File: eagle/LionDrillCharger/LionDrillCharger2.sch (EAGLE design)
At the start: 25 parts, among them IC1 AT90S2313P, K1 JW1A, K2 JW1A, K3 JW1A, K4 JW1A, T1 BC237, T2 BC237, T3 BC237, T4 BC237

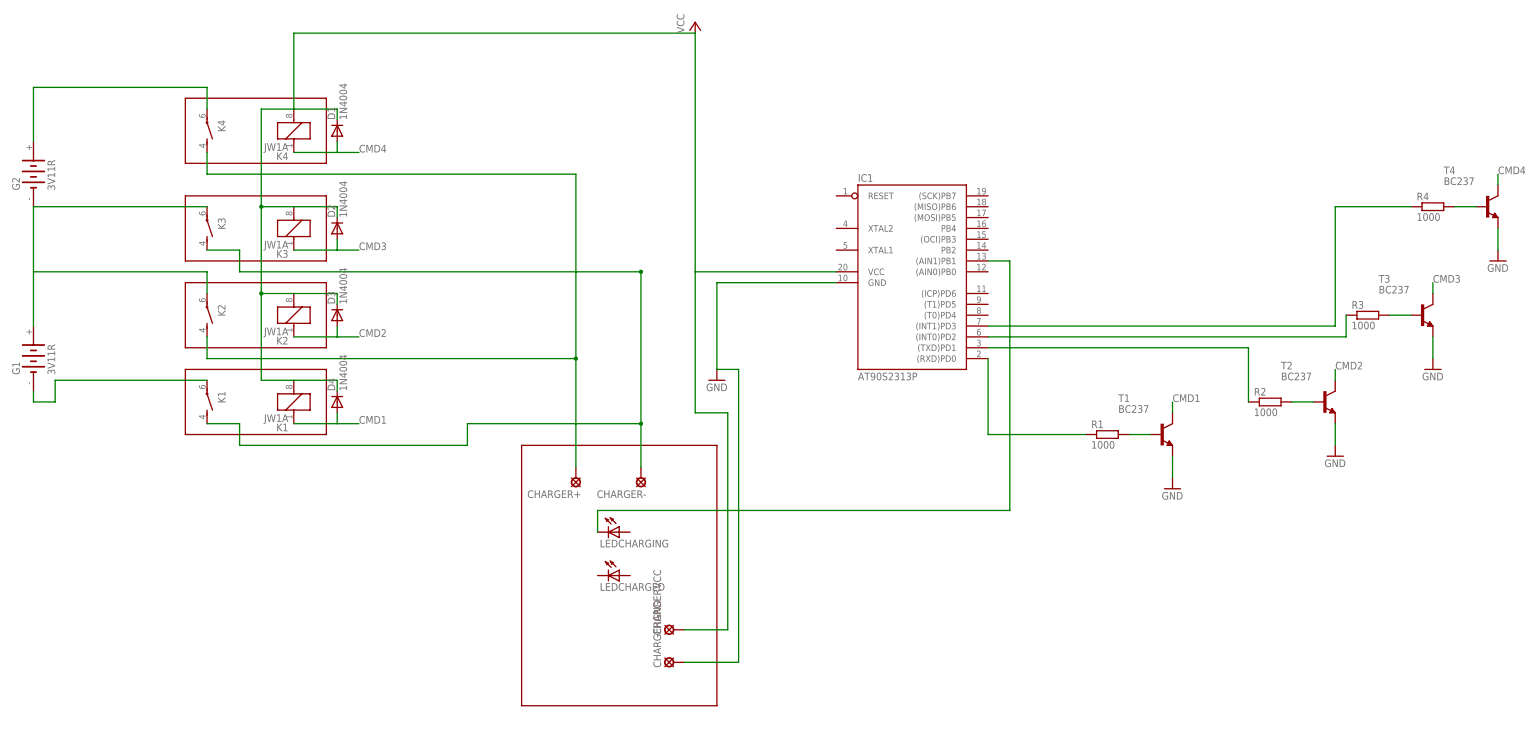
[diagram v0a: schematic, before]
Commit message: Added drill lion-charger schematics
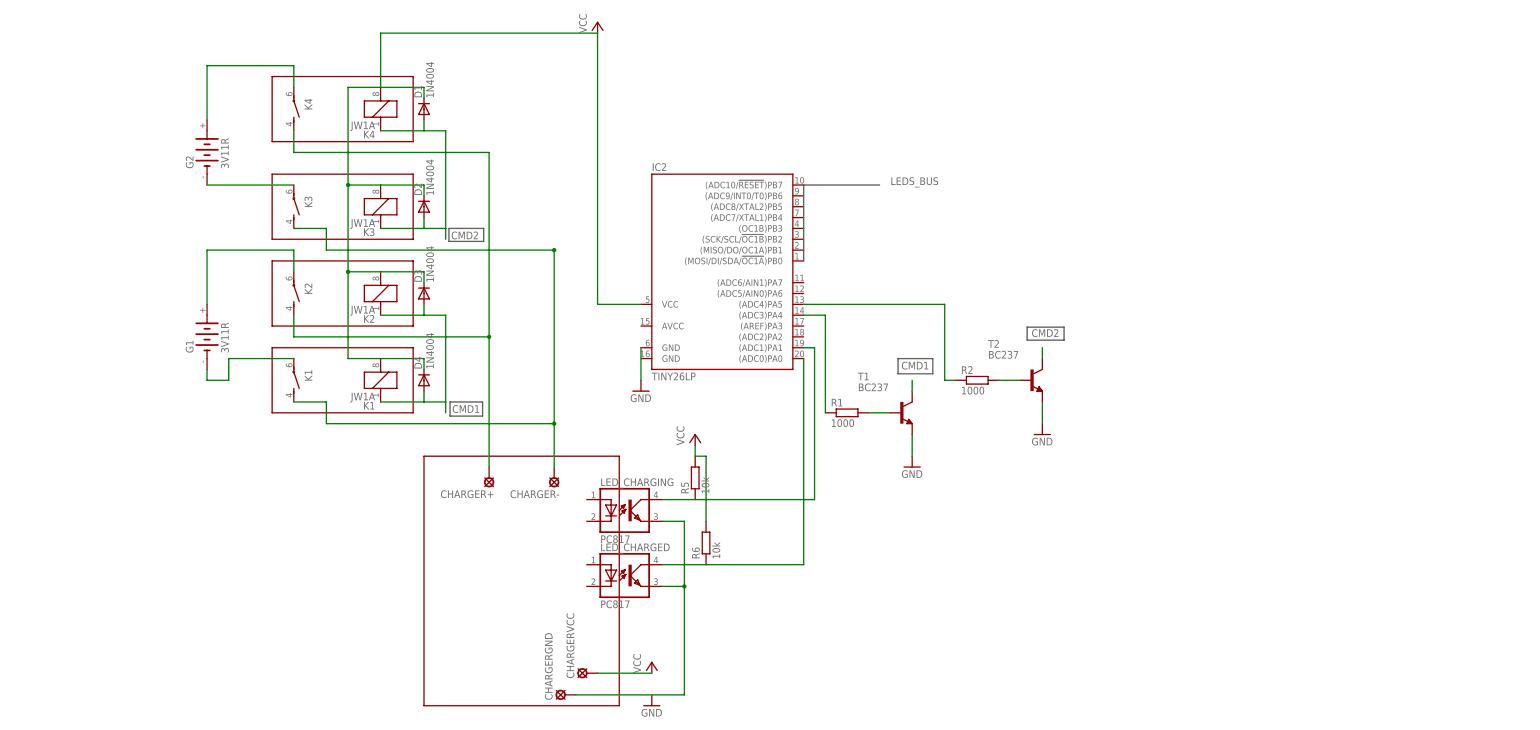
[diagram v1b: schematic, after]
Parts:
- removed IC1: AT90S2313P, atmel:AT90S2313P
- removed LEDCHARGED, LEDCHARGING: (no value), led:LED3MM
- removed R3, R4: 1000, resistor:R-EU_0204/5
- removed T3, T4: BC237, transistor:BC237
- added IC2: TINY26LP, atmel:TINY26LP
- added LED_CHARGED, LED_CHARGING: PC817, optocoupler:PC817
- added R5, R6: 10k, resistor:R-EU_0204/5
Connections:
- removed net CMD3: D2.A, K3_.1, T3.C
- removed net CMD4: D1.A, K4_.1, T4.C
- removed net N$10: R4.2, T4.B
- removed net N$13: IC1.(INT0)PD2, R3.1
- removed net N$14: IC1.(INT1)PD3, R4.1
- removed net N$15: IC1.(AIN1)PB1, LEDCHARGING.C
- removed net N$9: R3.2, T3.B
- new net N$16: CHARGERVCC.MP
- new net N$17: CHARGERGND.MP, LED_CHARGED.EMIT, LED_CHARGING.EMIT
- new net N$18: IC2.(ADC1)PA1, LED_CHARGING.COL, R5.1
- new net N$19: IC2.(ADC0)PA0, LED_CHARGED.COL, R6.1
- new net N$4: G1.+, K21.P
- net CMD1: now also D3.A, K2_.1
- net CMD2: now also D1.A, D2.A, K3_.1, K4_.1; no longer D3.A, K2_.1
- net GND: no longer CHARGERGND.MP, IC1.GND, T3.E, T4.E
- net N$11: no longer IC1.(RXD)PD0
- net N$12: no longer IC1.(TXD)PD1
- net N$6: no longer G1.+, K21.P
- net VCC: now also R5.2, R6.2; no longer CHARGERVCC.MP, IC1.VCC
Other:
- moved on the sheet: CHARGER+, CHARGER-, CHARGERGND, CHARGERVCC, D1, D2, D3, D4, G1, G2, K1, K2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
